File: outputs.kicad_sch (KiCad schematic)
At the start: 2 parts, among them J1 Conn_01x02_Socket, J6 Conn_01x04_Socket

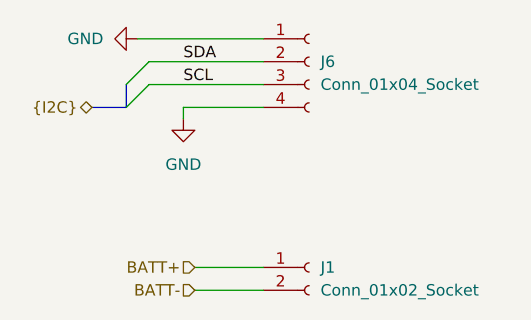
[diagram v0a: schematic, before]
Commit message: Adding in diodes and fixing circuit
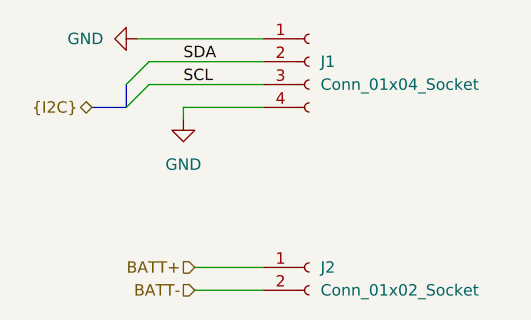
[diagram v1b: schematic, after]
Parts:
- renumbered J6 to J1, J1 to J2
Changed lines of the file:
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@@
 		(dnp no)
 		(fields_autoplaced yes)
-		(property "Reference" "#PWR03"
+		(property "Reference" "#PWR02"
 			(at 127 91.44 0)
 			(effects
@@
 			(project ""
 				(path "/124184ba-5d68-4d9f-8da6-acc6720ab30b/93f9b420-7cce-46a9-9201-666f07a18f85/2982e12c-39cd-4158-a648-a90b7f6b527c"
-					(reference "#PWR03")
+					(reference "#PWR02")
 					(unit 1)
 				)
@@
 		(dnp no)
 		(fields_autoplaced yes)
-		(property "Reference" "J6"
+		(property "Reference" "J1"
 			(at 142.24 78.7399 0)
 			(effects
@@
 			(project ""
 				(path "/124184ba-5d68-4d9f-8da6-acc6720ab30b/93f9b420-7cce-46a9-9201-666f07a18f85/2982e12c-39cd-4158-a648-a90b7f6b527c"
-					(reference "J6")
+					(reference "J1")
 					(unit 1)
 				)
@@
 		(dnp no)
 		(fields_autoplaced yes)
-		(property "Reference" "#PWR04"
+		(property "Reference" "#PWR01"
 			(at 115.57 76.2 0)
 			(effects
@@
 			(project ""
 				(path "/124184ba-5d68-4d9f-8da6-acc6720ab30b/93f9b420-7cce-46a9-9201-666f07a18f85/2982e12c-39cd-4158-a648-a90b7f6b527c"
-					(reference "#PWR04")
+					(reference "#PWR01")
 					(unit 1)
 				)
@@
 		(dnp no)
 		(fields_autoplaced yes)
-		(property "Reference" "J1"
+		(property "Reference" "J2"
 			(at 142.24 101.5999 0)
 			(effects
@@
 			(project ""
 				(path "/124184ba-5d68-4d9f-8da6-acc6720ab30b/93f9b420-7cce-46a9-9201-666f07a18f85/2982e12c-39cd-4158-a648-a90b7f6b527c"
-					(reference "J1")
+					(reference "J2")
 					(unit 1)
 				)
